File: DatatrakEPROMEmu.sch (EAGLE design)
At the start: 45 parts, among them IC1 LD1117AS33TR, IC2 XC95144XL_TQ144_P, Q1 BC847CSMD, Q2 BC847CSMD, Q3 BC847CSMD, U1 SN74LVCH16T245DGGR, U2 SN74LVCH16T245DGGR, U3 SN74LVCH16T245DGGR, U4 IS62WV25616DBLL-45TLI, U5 FT240XS, X1 MABC48B2, X2 PN61729-S

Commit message: add net labels, remove TODOs
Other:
- note removed: "TODO: Route FTDI I/F"
- note removed: "TODO: Status LEDs"
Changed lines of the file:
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@@
 <description>CPLD</description>
 <plain>
-<text x="20.32" y="228.6" size="5.08" layer="91">TODO: Route FTDI I/F</text>
 <text x="327.66" y="208.28" size="3.81" layer="97">JTAG</text>
-<text x="292.1" y="157.48" size="1.778" layer="91">TODO: Status LEDs</text>
 </plain>
 <instances>
@@
 <wire x1="109.22" y1="88.9" x2="83.82" y2="88.9" width="0.1524" layer="91"/>
 <wire x1="83.82" y1="88.9" x2="81.28" y2="91.44" width="0.1524" layer="91"/>
+<label x="86.36" y="88.9" size="1.778" layer="95"/>
 </segment>
 </net>
@@
 <wire x1="109.22" y1="119.38" x2="83.82" y2="119.38" width="0.1524" layer="91"/>
 <wire x1="83.82" y1="119.38" x2="81.28" y2="121.92" width="0.1524" layer="91"/>
+<label x="86.36" y="119.38" size="1.778" layer="95"/>
 </segment>
 </net>
@@
 <wire x1="109.22" y1="124.46" x2="83.82" y2="124.46" width="0.1524" layer="91"/>
 <wire x1="83.82" y1="124.46" x2="81.28" y2="127" width="0.1524" layer="91"/>
+<label x="86.36" y="124.46" size="1.778" layer="95"/>
 </segment>
 </net>
@@
 <wire x1="109.22" y1="127" x2="83.82" y2="127" width="0.1524" layer="91"/>
 <wire x1="83.82" y1="127" x2="81.28" y2="129.54" width="0.1524" layer="91"/>
+<label x="86.36" y="127" size="1.778" layer="95"/>
 </segment>
 </net>
@@
 <wire x1="109.22" y1="129.54" x2="83.82" y2="129.54" width="0.1524" layer="91"/>
 <wire x1="83.82" y1="129.54" x2="81.28" y2="132.08" width="0.1524" layer="91"/>
+<label x="86.36" y="129.54" size="1.778" layer="95"/>
 </segment>
 </net>
@@
 <wire x1="109.22" y1="132.08" x2="83.82" y2="132.08" width="0.1524" layer="91"/>
 <wire x1="83.82" y1="132.08" x2="81.28" y2="134.62" width="0.1524" layer="91"/>
+<label x="86.36" y="132.08" size="1.778" layer="95"/>
 </segment>
 </net>
@@
 <wire x1="109.22" y1="134.62" x2="83.82" y2="134.62" width="0.1524" layer="91"/>
 <wire x1="83.82" y1="134.62" x2="81.28" y2="137.16" width="0.1524" layer="91"/>
+<label x="86.36" y="134.62" size="1.778" layer="95"/>
 </segment>
 </net>
@@
 <wire x1="109.22" y1="137.16" x2="83.82" y2="137.16" width="0.1524" layer="91"/>
 <wire x1="83.82" y1="137.16" x2="81.28" y2="139.7" width="0.1524" layer="91"/>
+<label x="86.36" y="137.16" size="1.778" layer="95"/>
 </segment>
 </net>
@@
 <wire x1="109.22" y1="139.7" x2="83.82" y2="139.7" width="0.1524" layer="91"/>
 <wire x1="83.82" y1="139.7" x2="81.28" y2="142.24" width="0.1524" layer="91"/>
+<label x="86.36" y="139.7" size="1.778" layer="95"/>
 </segment>
 </net>
@@
 <wire x1="109.22" y1="142.24" x2="83.82" y2="142.24" width="0.1524" layer="91"/>
 <wire x1="83.82" y1="142.24" x2="81.28" y2="144.78" width="0.1524" layer="91"/>
+<label x="86.36" y="142.24" size="1.778" layer="95"/>
 </segment>
 </net>
@@
 <wire x1="109.22" y1="144.78" x2="83.82" y2="144.78" width="0.1524" layer="91"/>
 <wire x1="83.82" y1="144.78" x2="81.28" y2="147.32" width="0.1524" layer="91"/>
+<label x="86.36" y="144.78" size="1.778" layer="95"/>
 </segment>
 </net>
@@
 <wire x1="109.22" y1="149.86" x2="83.82" y2="149.86" width="0.1524" layer="91"/>
 <wire x1="83.82" y1="149.86" x2="81.28" y2="152.4" width="0.1524" layer="91"/>
+<label x="86.36" y="149.86" size="1.778" layer="95"/>
 </segment>
 </net>
@@
 <wire x1="109.22" y1="152.4" x2="83.82" y2="152.4" width="0.1524" layer="91"/>
 <wire x1="83.82" y1="152.4" x2="81.28" y2="154.94" width="0.1524" layer="91"/>
+<label x="86.36" y="152.4" size="1.778" layer="95"/>
 </segment>
 </net>
@@
 <wire x1="109.22" y1="154.94" x2="83.82" y2="154.94" width="0.1524" layer="91"/>
 <wire x1="83.82" y1="154.94" x2="81.28" y2="157.48" width="0.1524" layer="91"/>
+<label x="86.36" y="154.94" size="1.778" layer="95"/>
 </segment>
 </net>
@@
 <wire x1="109.22" y1="157.48" x2="83.82" y2="157.48" width="0.1524" layer="91"/>
 <wire x1="83.82" y1="157.48" x2="81.28" y2="160.02" width="0.1524" layer="91"/>
+<label x="86.36" y="157.48" size="1.778" layer="95"/>
 </segment>
 </net>
@@
 <wire x1="109.22" y1="160.02" x2="83.82" y2="160.02" width="0.1524" layer="91"/>
 <wire x1="83.82" y1="160.02" x2="81.28" y2="162.56" width="0.1524" layer="91"/>
+<label x="86.36" y="160.02" size="1.778" layer="95"/>
 </segment>
 </net>
@@
 <wire x1="109.22" y1="162.56" x2="83.82" y2="162.56" width="0.1524" layer="91"/>
 <wire x1="83.82" y1="162.56" x2="81.28" y2="165.1" width="0.1524" layer="91"/>
+<label x="86.36" y="162.56" size="1.778" layer="95"/>
 </segment>
 </net>
@@
 <wire x1="134.62" y1="187.96" x2="134.62" y2="210.82" width="0.1524" layer="91"/>
 <wire x1="134.62" y1="210.82" x2="132.08" y2="213.36" width="0.1524" layer="91"/>
+<label x="134.62" y="198.12" size="1.778" layer="95" rot="R90"/>
 </segment>
 </net>
@@
 <wire x1="137.16" y1="187.96" x2="137.16" y2="210.82" width="0.1524" layer="91"/>
 <wire x1="137.16" y1="210.82" x2="134.62" y2="213.36" width="0.1524" layer="91"/>
+<label x="137.16" y="198.12" size="1.778" layer="95" rot="R90"/>
 </segment>
 </net>
@@
 <wire x1="142.24" y1="187.96" x2="142.24" y2="210.82" width="0.1524" layer="91"/>
 <wire x1="142.24" y1="210.82" x2="139.7" y2="213.36" width="0.1524" layer="91"/>
+<label x="142.24" y="198.12" size="1.778" layer="95" rot="R90"/>
 </segment>
 </net>
@@
 <wire x1="144.78" y1="187.96" x2="144.78" y2="210.82" width="0.1524" layer="91"/>
 <wire x1="144.78" y1="210.82" x2="142.24" y2="213.36" width="0.1524" layer="91"/>
+<label x="144.78" y="198.12" size="1.778" layer="95" rot="R90"/>
 </segment>
 </net>
@@
 <wire x1="147.32" y1="187.96" x2="147.32" y2="210.82" width="0.1524" layer="91"/>
 <wire x1="147.32" y1="210.82" x2="144.78" y2="213.36" width="0.1524" layer="91"/>
+<label x="147.32" y="198.12" size="1.778" layer="95" rot="R90"/>
 </segment>
 </net>
@@
 <wire x1="149.86" y1="187.96" x2="149.86" y2="210.82" width="0.1524" layer="91"/>
 <wire x1="149.86" y1="210.82" x2="147.32" y2="213.36" width="0.1524" layer="91"/>
+<label x="149.86" y="198.12" size="1.778" layer="95" rot="R90"/>
 </segment>
 </net>
@@
 <wire x1="152.4" y1="187.96" x2="152.4" y2="210.82" width="0.1524" layer="91"/>
 <wire x1="152.4" y1="210.82" x2="149.86" y2="213.36" width="0.1524" layer="91"/>
-</segment>
-</net>
+<label x="152.4" y="198.12" size="1.778" layer="95" rot="R90"/>
+</segment>
+</net>

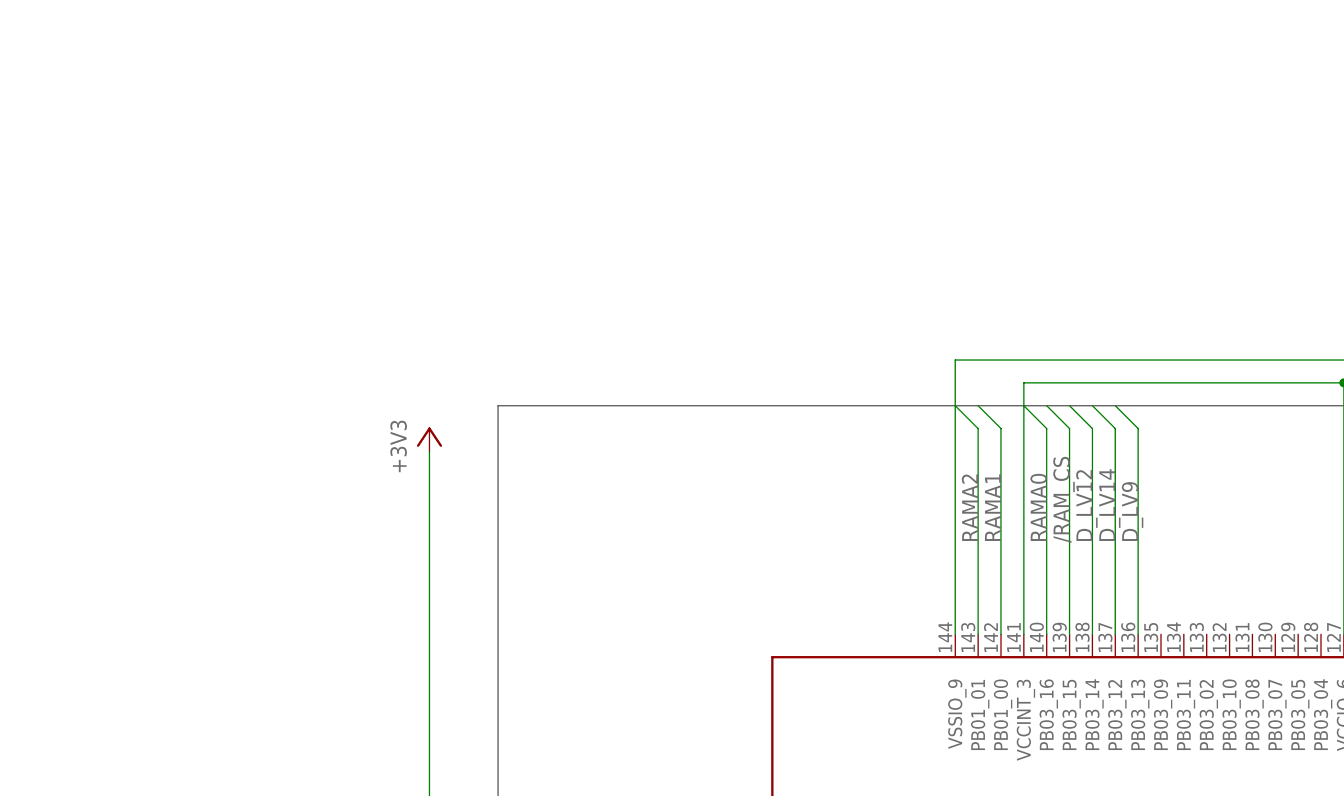
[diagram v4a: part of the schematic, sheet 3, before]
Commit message: add missing D_LV8 net between CPLD and SRAM/translator
OSHPark PCBs had a missing net -- D_LV8 -- the 8th data bit from the level
translator to the CPLD. These boards will need a greenwire.
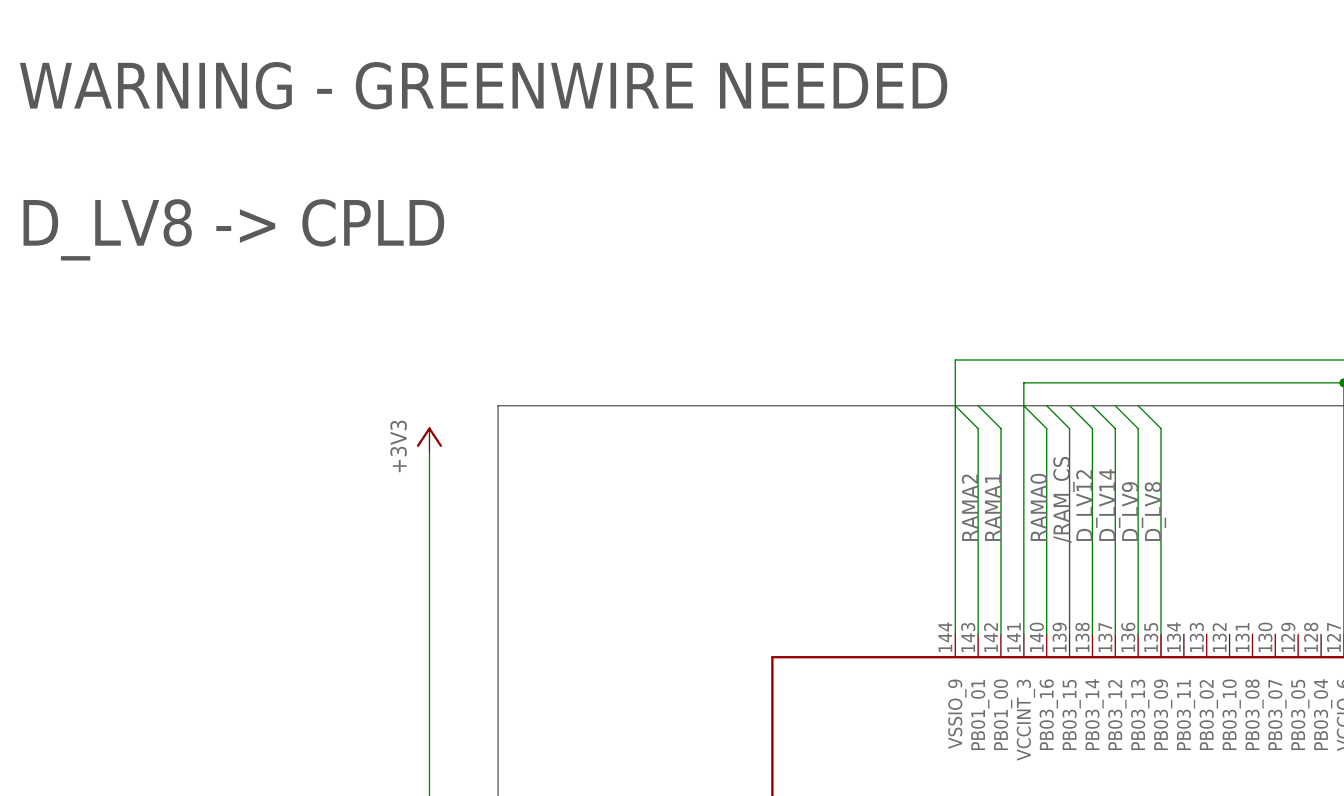
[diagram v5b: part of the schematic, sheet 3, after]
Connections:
- net D_LV8: now also IC2.PB03_09
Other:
- note added: "WARNING - GREENWIRE NEEDED D_LV8 -> CPLD"
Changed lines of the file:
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@@
 <plain>
 <text x="327.66" y="208.28" size="3.81" layer="97">JTAG</text>
+<text x="27.94" y="231.14" size="5.08" layer="97">WARNING - GREENWIRE NEEDED
+D_LV8 -&gt; CPLD</text>
 </plain>
 <instances>
@@
 </segment>
 </net>
+<net name="D_LV8" class="0">
+<segment>
+<pinref part="IC2" gate="G$1" pin="PB03_09"/>
+<wire x1="154.94" y1="187.96" x2="154.94" y2="210.82" width="0.1524" layer="91"/>
+<wire x1="154.94" y1="210.82" x2="152.4" y2="213.36" width="0.1524" layer="91"/>
+<label x="154.94" y="198.12" size="1.778" layer="95" rot="R90"/>
+</segment>
+</net>

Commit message: Add TODO - original Datatrak ROM board had two separate ROMs, do we need split hi/lo data enables?
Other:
- note added: "TODO: Target Data Enable is wordwise, not bytewise. Is this a problem? Do we need a High DEN and Low DEN gated from OEL and OEH?"
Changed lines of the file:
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@@
 <text x="289.56" y="33.02" size="2.54" layer="97" rot="MR180">EPROM emulator for Datatrak Mk2 Locator
   Target I/O and level translation</text>
+<text x="127" y="144.78" size="5.08" layer="97">TODO: Target Data Enable is wordwise, not bytewise.
+Is this a problem?
+Do we need a High DEN and Low DEN gated from OEL and OEH?</text>
 </plain>
 <instances>
